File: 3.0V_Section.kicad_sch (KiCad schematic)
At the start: 2 parts, among them U1_15 ADP7104ARDZ-R7, U2_8 TPL0102-100PWR

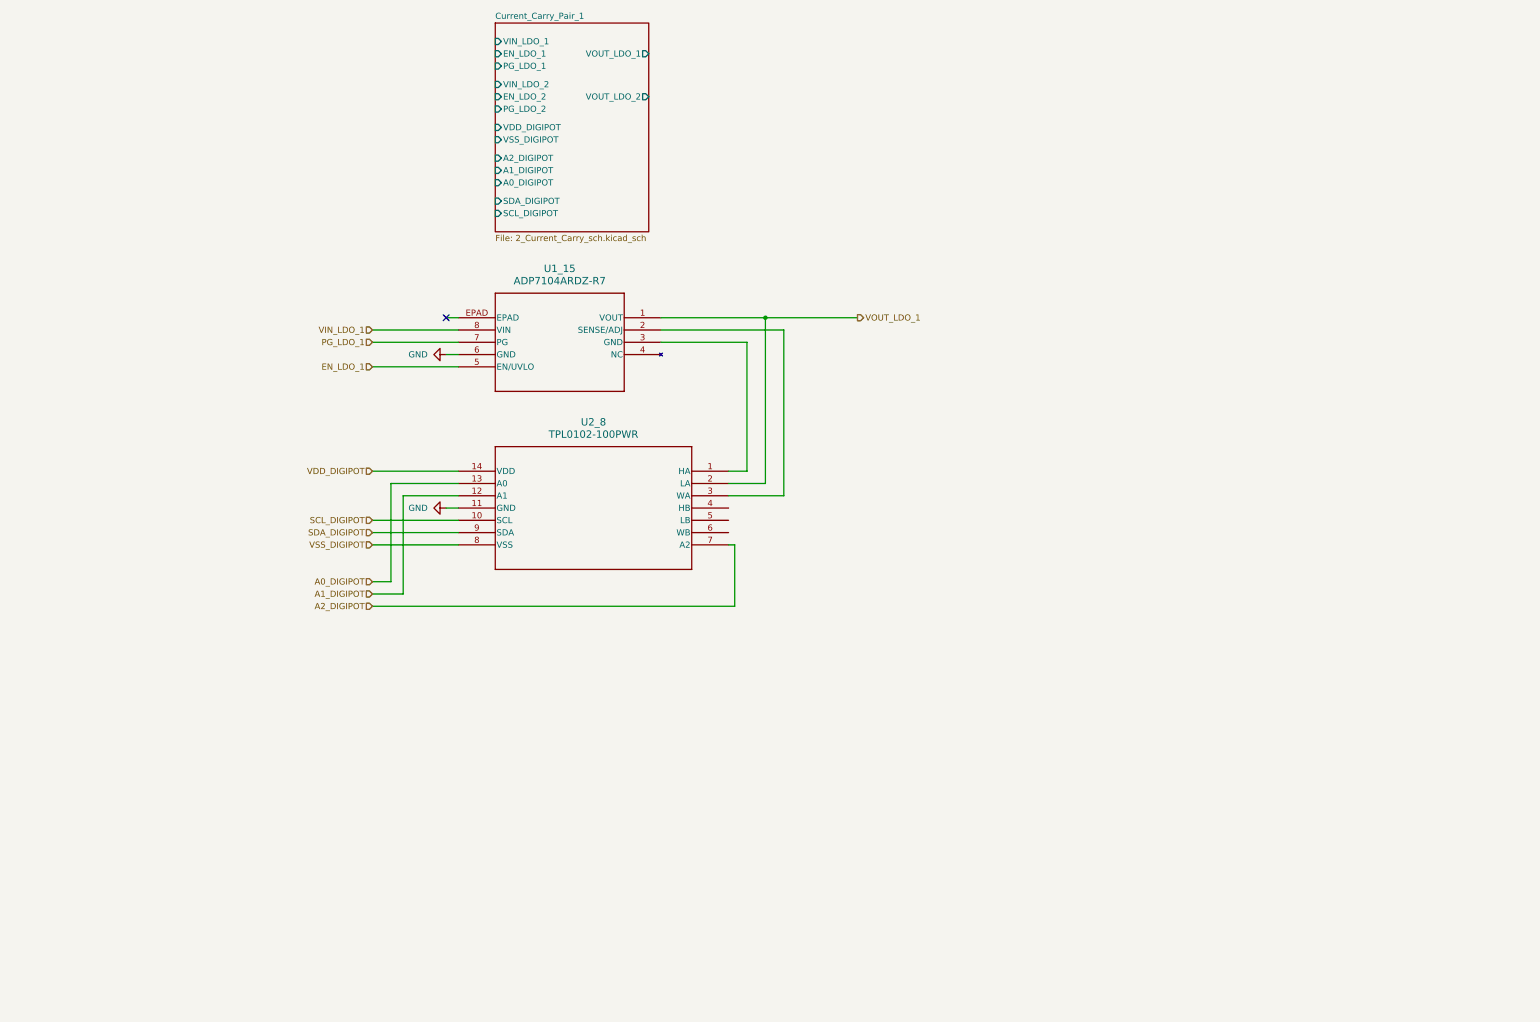
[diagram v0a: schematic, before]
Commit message: Full schematic connection without ratio consideration.
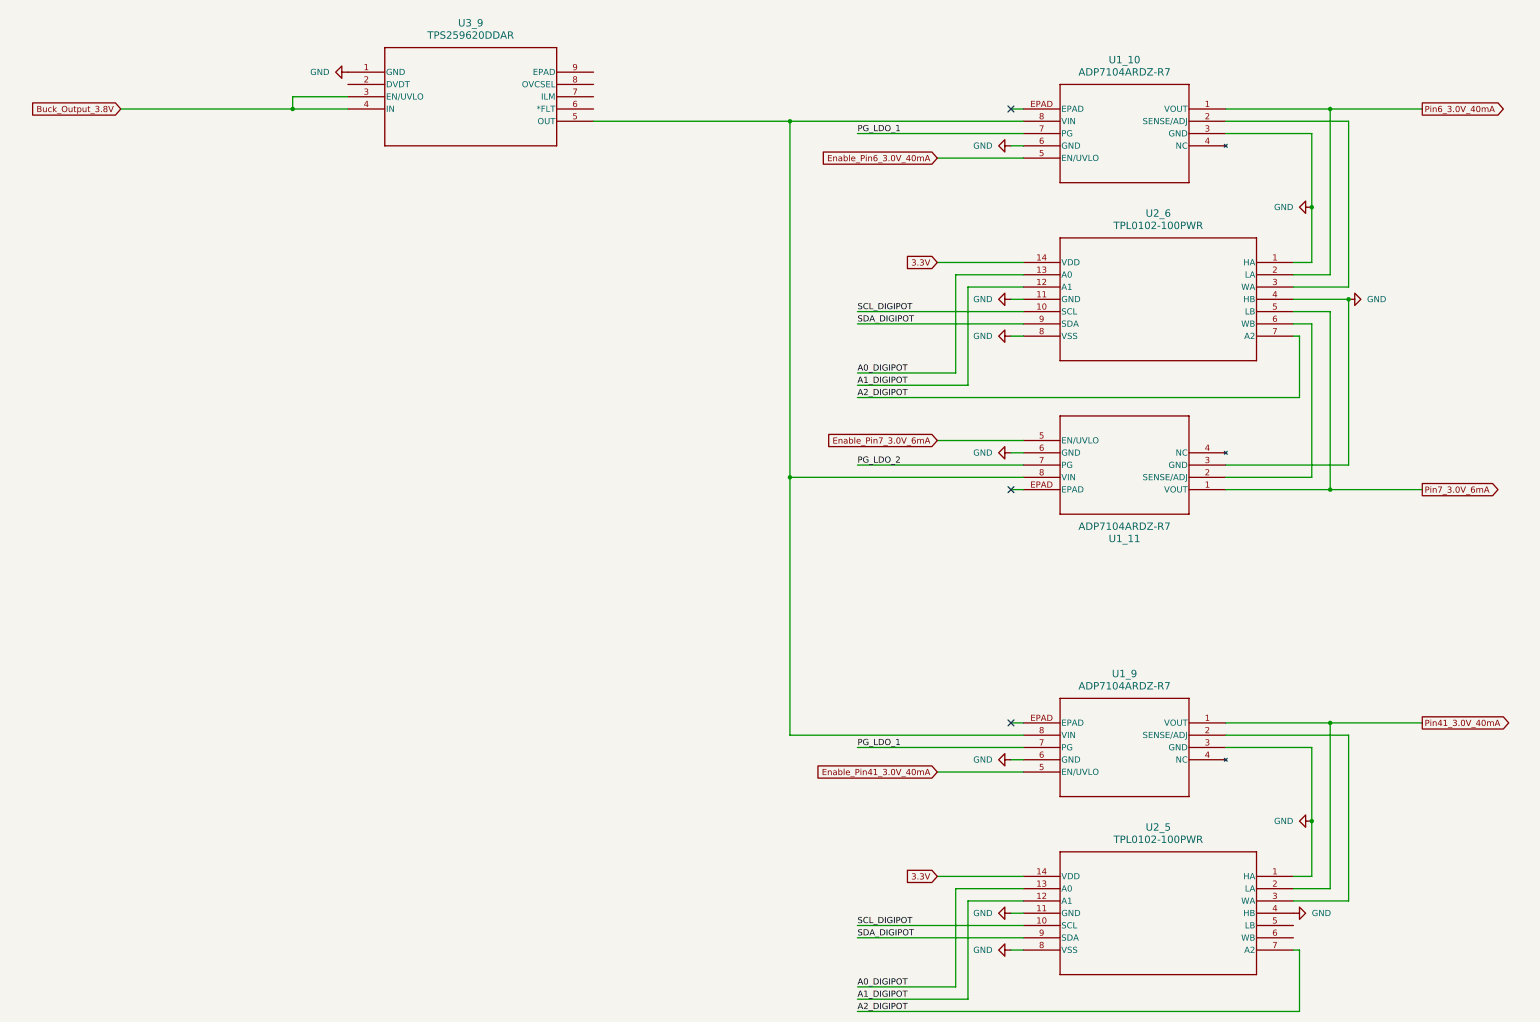
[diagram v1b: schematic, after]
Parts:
- added U1_10, U1_11: ADP7104ARDZ-R7, RD_8_2_ADI, symbol Adjustable Low-Dropout Regulator:ADP7104ARDZ-R7
- added U2_6: TPL0102-100PWR, PW14, symbol Digital Potentiometer:TPL0102-100PWR
- added U3_9: TPS259620DDAR, SOIC_20DDAR_TEX, symbol eFuse for electronic:TPS259620DDAR
- renumbered U1_15 to U1_9, U2_8 to U2_5
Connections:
- net VSS_DIGIPOT is gone; now on net GND: U2_5.8 (VSS)
- net A0_DIGIPOT: now also U2_6.13 (A0)
- net A1_DIGIPOT: now also U2_6.12 (A1)
- net A2_DIGIPOT: now also U2_6.7 (A2)
- net GND: now also U1_9.3 (GND), U2_5.1 (HA), U2_5.4 (HB), U1_10.3 (GND), U1_10.6 (GND), U1_11.3 (GND), U1_11.6 (GND), U2_6.1 (HA), U2_6.11 (GND), U2_6.4 (HB), U2_6.8 (VSS), U3_9.1 (GND)
- net PG_LDO_1: now also U1_10.7 (PG)
- net SCL_DIGIPOT: now also U2_6.10 (SCL)
- net SDA_DIGIPOT: now also U2_6.9 (SDA)
- net EN_LDO_1 renamed Enable_Pin41_3.0V_40mA
- net VDD_DIGIPOT renamed 3.3V
- net 3.3V: now also U2_6.14 (VDD)
- net VIN_LDO_1: no longer names the net of U1_9.8 (VIN)
- net VIN_LDO_1: now also U1_10.8 (VIN), U1_11.8 (VIN), U3_9.5 (OUT)
- net VOUT_LDO_1 renamed Pin41_3.0V_40mA
- new net: U1_10.2 (SENSE/ADJ), U2_6.3 (WA)
- new net: U1_11.2 (SENSE/ADJ), U2_6.6 (WB)
- new net Buck_Output_3.8V: U3_9.3 (EN/UVLO), U3_9.4 (IN)
- new net Enable_Pin6_3.0V_40mA: U1_10.5 (EN/UVLO)
- new net Enable_Pin7_3.0V_6mA: U1_11.5 (EN/UVLO)
- new net PG_LDO_2: U1_11.7 (PG)
- new net Pin6_3.0V_40mA: U1_10.1 (VOUT), U2_6.2 (LA)
- new net Pin7_3.0V_6mA: U1_11.1 (VOUT), U2_6.5 (LB)
- no-connect marks 1 -> 3
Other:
- removed sheet Current_Carry_Pair_1
- moved on the sheet: U1_9, U2_5
